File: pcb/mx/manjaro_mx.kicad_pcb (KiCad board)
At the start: 2 copper layers, 285.8 x 101 mm, 91 parts, among them SW1 SW_Push, SW10 SW_Push, SW11 SW_Push, SW12 SW_Push, SW13 SW_Push, SW14 SW_Push, SW15 SW_Push, SW16 SW_Push, SW17 SW_Push, SW18 SW_Push, SW19 SW_Push, SW2 SW_Push, SW20 SW_Push, SW21 SW_Push, SW22 SW_Push, SW3 SW_Push, SW4 SW_Push, SW5 SW_Push, SW6 SW_Push, SW7 SW_Push, SW8 SW_Push, SW9 SW_Push, U1 XIAO-RP2040-DIP

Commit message: [V0] add jlcpcb files
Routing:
- net rBAT-: track 182.9 -> 177.8 mm
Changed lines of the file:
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@@
 		(sheetname "ルート")
 		(sheetfile "manjaro_mx.kicad_sch")
-		(attr through_hole)
+		(attr through_hole exclude_from_bom dnp)
 		(fp_line
 			(start -2.06 -1.46)
@@
 		(sheetname "ルート")
 		(sheetfile "manjaro_mx.kicad_sch")
-		(attr through_hole)
+		(attr through_hole exclude_from_bom dnp)
 		(fp_line
 			(start -1.33 -1.33)
@@
 		(tags "connector JST PH top entry")
 		(property "Reference" "rBT1"
-			(at 1 -2.55 360)
+			(at 1 -2.55 0)
 			(layer "F.SilkS")
 			(effects
@@
 		)
 		(property "Value" "Battery_Cell"
-			(at 1 7.45 360)
+			(at 1 7.45 0)
 			(layer "F.Fab")
 			(effects
@@
 		(sheetname "ルート")
 		(sheetfile "manjaro_mx.kicad_sch")
-		(attr through_hole)
+		(attr through_hole exclude_from_bom dnp)
 		(fp_line
 			(start -2.06 -1.46)
@@
 		)
 		(fp_text user "${REFERENCE}"
-			(at 1 2.5 360)
+			(at 1 2.5 0)
 			(layer "F.Fab")
 			(effects
@@
 		)
 		(property "Value" "SW_Push"
-			(at 0.000001 7.8 15)
+			(at 0.000002 7.8 15)
 			(layer "B.Fab")
 			(hide yes)
@@
 				(xy 5.25 5.65) (xy 5.4 5.4) (xy 5.5 5) (xy 5.5 4.6) (xy 5.35 4.5) (xy 5.2 4.4) (xy 4.75 4.65) (xy 4.5 4.75)
 				(xy 4.05 4.85) (xy 3.55 4.85) (xy 2.95 4.7) (xy 2.45 4.4) (xy 2.15 4.15) (xy 1.75 3.6) (xy 1.55 3.05)
-				(xy 1.5 2.6) (xy 1.25 2.800001) (xy 0.899999 2.9) (xy 0.4 2.950001) (xy -1.65 2.95) (xy -1.2 3.2)
+				(xy 1.5 2.6) (xy 1.25 2.800001) (xy 0.899999 2.9) (xy 0.4 2.950002) (xy -1.65 2.95) (xy -1.2 3.2)
 				(xy -0.95 3.4) (xy -0.65 3.75) (xy -0.5 4) (xy -0.35 4.35) (xy -0.25 4.75) (xy -0.25 5.05) (xy -0.25 5.4)
 				(xy -0.3 5.65) (xy -0.45 6.05) (xy -0.75 6.5)
@@
 	)
 	(segment
-		(start 280 127.165)
-		(end 281.15 126.015)
+		(start 281.15 126.015)
+		(end 280 127.165)
 		(width 0.2)
 		(layer "B.Cu")
@@
 	)
 	(segment
-		(start 281.15 136.175)
-		(end 280 135.025)
+		(start 201.75 77.25)
+		(end 201.75 80)
 		(width 0.2)
 		(layer "B.Cu")
@@
 	)
 	(segment
-		(start 201.75 77.25)
-		(end 201.75 80)
+		(start 280 132.485)
+		(end 281.15 133.635)
 		(width 0.2)
 		(layer "B.Cu")
@@
 	)
 	(segment
-		(start 280 135.025)
-		(end 280 127.165)
-		(width 0.2)
-		(layer "B.Cu")
-		(net 27)
-	)
-	(segment
 		(start 191 82.46)
 		(end 191 106)
@@
 	)
 	(segment
-		(start 281.15 136.175)
-		(end 281.15 133.635)
+		(start 280 127.165)
+		(end 280 132.485)
 		(width 0.2)
 		(layer "B.Cu")

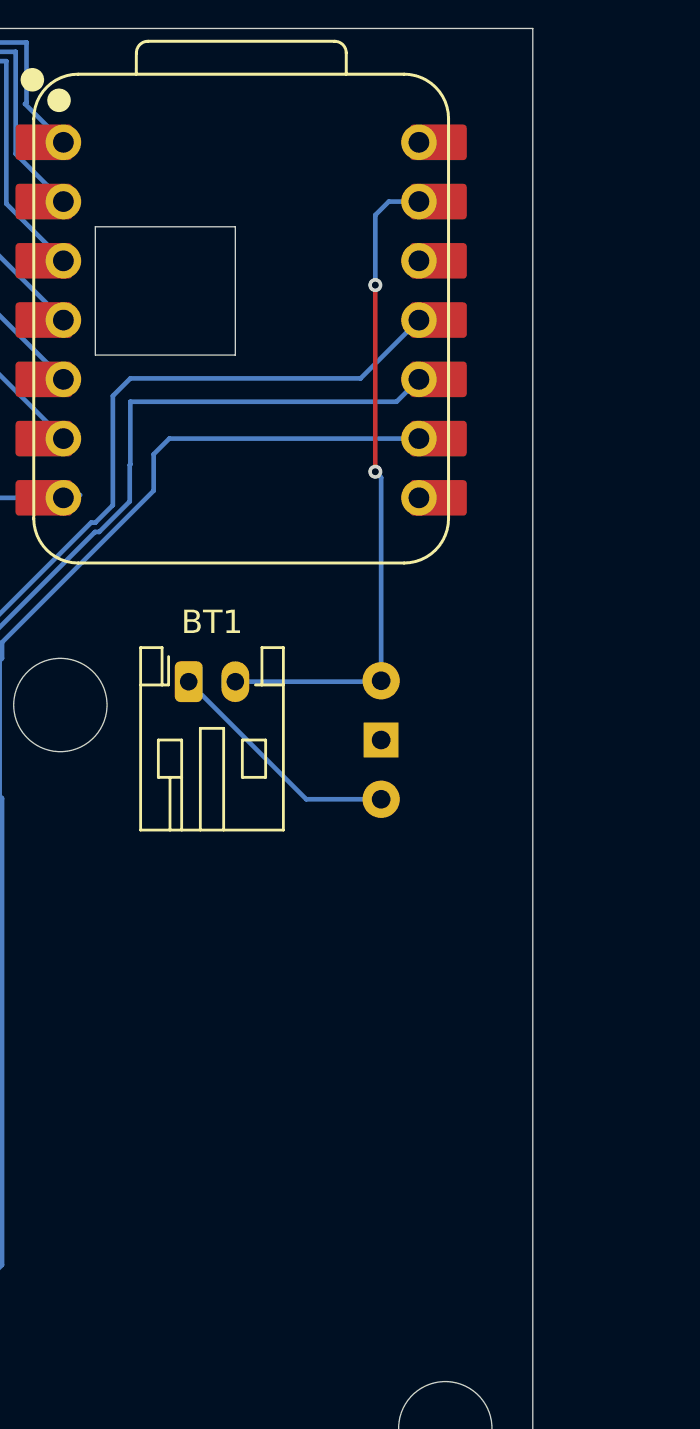
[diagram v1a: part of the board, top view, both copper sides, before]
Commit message: [V0] Add TRRS conn for mint right
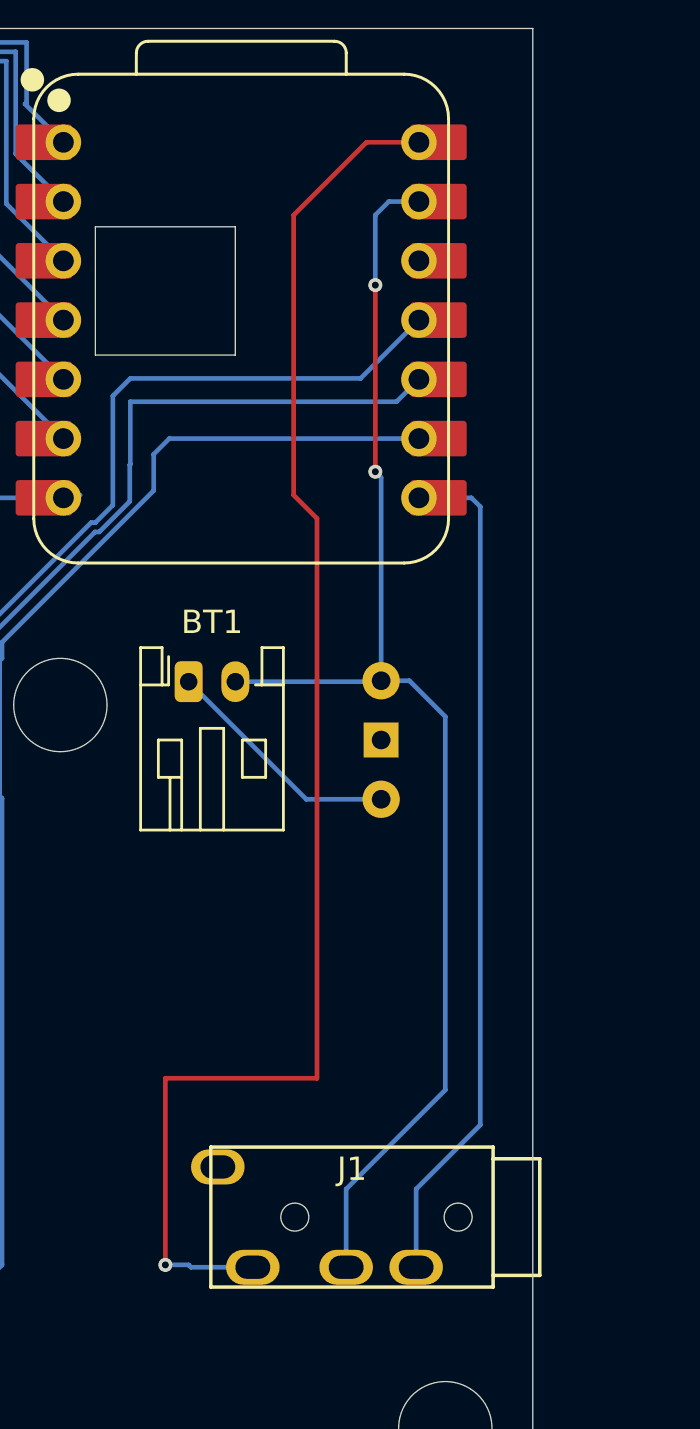
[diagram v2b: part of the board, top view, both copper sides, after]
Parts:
- added J1: MJ-4PP-9, MJ-4PP-9:MJ-4PP-9, F.Cu at (172.0, 103.0)
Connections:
- U1 pad 14: unconnected-(U1-VBUS-Pad14)_0 -> 5V
- U1 pad 8: unconnected-(U1-P1.12_RX_D7-Pad8)_0 -> TX
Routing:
- net 5V: track 0.00 -> 63.2 mm, vias 0 -> 1
- net TX: track 0.00 -> 36.5 mm
- net BAT-: track 28.4 -> 57.2 mm

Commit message: Modify key layout
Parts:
- removed J1: MJ-4PP-9, MJ-4PP-9:MJ-4PP-9
- added D23: 1N4148WT, digikey-footprints:SOD-523, B.Cu at (63.5, 140.2)
- added D24: 1N4148WT, digikey-footprints:SOD-523, B.Cu at (44.5, 142.2)
- added SW23: SW_Push, kbd_SW:CherryMX_Choc_Hotswap_1u, F.Cu at (69.0, 131.2)
- added SW24: SW_Push, kbd_SW:CherryMX_Choc_Hotswap_1u, F.Cu at (50.0, 133.2)
- added rD21: 1N4148WT, digikey-footprints:SOD-523, B.Cu at (291.7, 140.2)
- added rD22: 1N4148WT, digikey-footprints:SOD-523, B.Cu at (310.8, 142.2)
- added rSW21: SW_Push, kbd_SW:CherryMX_Choc_Hotswap_1u, F.Cu at (297.2, 131.2)
- added rSW22: SW_Push, kbd_SW:CherryMX_Choc_Hotswap_1u, F.Cu at (316.2, 133.2)
- D1, D10, D11, D12, D13, D14, D15, D16, D17, D18, D19, D2, D20, D21, D22, D3, D4, D5, D6, D7, D8, D9, rD1, rD10, rD11, rD12, rD13, rD14, rD15, rD16, rD17, rD18, rD19, rD2, rD20, rD3, rD4, rD5, rD6, rD7, rD8, rD9: footprint Diode_SMD:D_SOD-523 -> digikey-footprints:SOD-523
- SW1, SW10, SW11, SW12, SW13, SW14, SW15, SW16, SW17, SW18, SW19, SW2, SW20, SW21, SW22, SW3, SW4, SW5, SW6, SW7, SW8, SW9, rSW1, rSW10, rSW11, rSW12, rSW13, rSW14, rSW15, rSW16, rSW17, rSW18, rSW19, rSW2, rSW20, rSW3, rSW4, rSW5, rSW6, rSW7, rSW8, rSW9: footprint kbd:keyswitch_cherrymx_hotswap_1u -> kbd_SW:CherryMX_Choc_Hotswap_1u; moved to F.Cu
- U1, rU1: value XIAO-RP2040-DIP -> nice_nano; footprint Seeed Studio XIAO Series Library:XIAO-RP2040-DIP -> nice-nano-kicad:nice_nano
- moved rD19 119.5 mm to (205.8, 146.7), turned to 24 degrees
- moved rSW19 118.6 mm to (206.1, 136.1), turned to 24 degrees
- moved rSW6 95.3 mm to (316.2, 76.0), turned to 0 degrees
- moved rD6 89.7 mm to (310.8, 85.0)
- moved rSW16 87.1 mm to (278.1, 99.1), turned to 0 degrees
- moved rSW17 79.6 mm to (297.2, 112.1), turned to 0 degrees
- moved rD16 77.7 mm to (272.6, 108.1), turned to 180 degrees
- moved rSW11 76.7 mm to (297.2, 93.0), turned to 0 degrees
- moved rSW12 76.3 mm to (316.2, 95.0), turned to 0 degrees
- moved rD17 71.5 mm to (291.7, 121.1), turned to 180 degrees
- moved rD11 71.1 mm to (291.7, 102.0)
- moved rD12 70.4 mm to (310.8, 104.0)
- moved rD20 62.1 mm to (272.6, 127.2)
- moved rSW20 58.3 mm to (278.1, 118.2), turned to 0 degrees
- moved rD15 47.0 mm to (253.6, 104.1)
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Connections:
- U1 pad 1: COL5 -> unconnected-(U1-TX0/P0.06-Pad1)
- U1 pad 10: ROW2 -> COL3
- U1 pad 11: ROW1 -> COL4
- U1 pad 12: unconnected-(U1-3V3-Pad12) -> COL5
- U1 pad 13: BAT- -> unconnected-(U1-NFC1/P0.09-Pad13)
- U1 pad 14: 5V -> unconnected-(U1-NFC2/P0.10-Pad14)
- U1 pad 2: COL4 -> unconnected-(U1-RX1/P0.08-Pad2)
- U1 pad 3: COL3 -> BAT-
- U1 pad 4: COL2 -> BAT-
- U1 pad 5: COL1 -> unconnected-(U1-P0.17-Pad5)
- U1 pad 6: COL0 -> unconnected-(U1-P0.20-Pad6)
- U1 pad 7: ROW0 -> COL0
- U1 pad 8: TX -> COL1
- U1 pad 9: ROW3 -> COL2
- rJ3 pad 1: 3V3 -> r3V3
- rJ3 pad 5: rBAT- -> nCS
- rSW10 pad 2: rCOL4 -> rCOL3
- rSW11 pad 2: rCOL0 -> rCOL4
- rSW12 pad 2: rCOL1 -> rCOL5
- rSW13 pad 2: rCOL2 -> rCOL0
- rSW14 pad 2: rCOL3 -> rCOL1
- rSW15 pad 2: rCOL4 -> rCOL2
- rSW16 pad 2: rCOL0 -> rCOL3
- rSW17 pad 2: rCOL1 -> rCOL4
- rSW18 pad 2: rCOL2 -> rCOL5
- rSW19 pad 2: rCOL3 -> rCOL0
- rSW20 pad 2: rCOL4 -> rCOL1
- rSW6 pad 2: rCOL0 -> rCOL5
- rSW7 pad 2: rCOL1 -> rCOL0
- rSW8 pad 2: rCOL2 -> rCOL1
- rSW9 pad 2: rCOL3 -> rCOL2
- rU1 pad 1: rROW1 -> unconnected-(rU1-TX0/P0.06-Pad1)
- rU1 pad 10: rROW2 -> rCOL3
- rU1 pad 11: SDIO -> rCOL4
- rU1 pad 12: 3V3 -> rCOL5
- rU1 pad 13: rBAT- -> unconnected-(rU1-NFC1/P0.09-Pad13)
- rU1 pad 2: rCOL4 -> unconnected-(rU1-RX1/P0.08-Pad2)
- rU1 pad 3: rCOL3 -> rBAT-
- rU1 pad 4: rCOL2 -> rBAT-
- rU1 pad 5: rCOL1 -> unconnected-(rU1-P0.17-Pad5)
- rU1 pad 6: rCOL0 -> unconnected-(rU1-P0.20-Pad6)
- rU1 pad 7: rROW0 -> rCOL0
- rU1 pad 8: rROW3 -> rCOL1
- rU1 pad 9: SCLK -> rCOL2
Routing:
- net rROW3: track 258.2 -> 0.00 mm, vias 8 -> 0
- net rCOL2: track 202.2 -> 0.00 mm, vias 4 -> 0
- net rCOL3: track 196.9 -> 0.00 mm, vias 4 -> 0
- net rCOL4: track 195.8 -> 0.00 mm
- net rBAT-: track 177.8 -> 0.00 mm, vias 2 -> 0
- net COL3: track 176.8 -> 0.00 mm
- net ROW3: track 176.8 -> 0.00 mm, vias 8 -> 0
- net COL5: track 175.4 -> 0.00 mm, vias 2 -> 0
- net ROW2: track 175.0 -> 0.00 mm, vias 8 -> 0
- net rROW1: track 168.4 -> 0.00 mm, vias 10 -> 0
- net 3V3: track 167.3 -> 0.00 mm, vias 1 -> 0
- net ROW1: track 165.7 -> 0.00 mm, vias 10 -> 0
- net COL2: track 160.4 -> 0.00 mm
- net COL4: track 159.7 -> 0.00 mm, vias 2 -> 0
- net rCOL1: track 153.4 -> 0.00 mm, vias 2 -> 0
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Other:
- board size 285.8 x 101 mm -> 289 x 116 mm
- board text added: "Manjaro v1"

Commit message: Modify MCU position
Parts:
- added EXSW1: RotaryEncoder_Switch, Keebio-Parts:RotaryEncoder_EC11, F.Cu at (164.3, 108.1)
- added rEXSW1: RotaryEncoder_Switch, Keebio-Parts:RotaryEncoder_EC11, F.Cu at (201.9, 108.1)
- moved U1 107.3 mm to (60.0, 56.0), turned to 0 degrees
- moved rU1 106.3 mm to (306.0, 56.0), turned to 180 degrees
- moved rPowerSW1 62.4 mm to (240.1, 51.0), turned to 0 degrees
- moved PowerSW1 62.2 mm to (126.2, 51.0), turned to 0 degrees
- moved rBT1 48.1 mm to (228.0, 51.0), turned to -90 degrees
- moved BT1 45.1 mm to (138.2, 53.0), turned to 90 degrees
- moved rJ3 7.88 mm to (262.0, 130.8)
- moved SW20 3.16 mm to (137.2, 130.1), turned to 0 degrees
- moved D1 3.00 mm to (139.8, 79.0)
- moved D13 3.00 mm to (139.8, 117.1)
- moved D19 3.00 mm to (151.8, 140.3), turned to 165 degrees
- moved D7 3.00 mm to (139.8, 98.0)
- moved SW1 3.00 mm to (145.2, 70.0)
- moved SW13 3.00 mm to (145.2, 108.1)
- moved SW19 3.00 mm to (160.2, 133.1), turned to -15 degrees
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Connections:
- U1 pad 15: unconnected-(U1-P1.11-Pad15) -> KEYEX1
- U1 pad 5: unconnected-(U1-P0.17-Pad5) -> REB
- U1 pad 6: unconnected-(U1-P0.20-Pad6) -> RE0A
- rU1 pad 15: unconnected-(rU1-P1.11-Pad15) -> rKEYEX1
- rU1 pad 5: unconnected-(rU1-P0.17-Pad5) -> rREB
- rU1 pad 6: unconnected-(rU1-P0.20-Pad6) -> rRE0A
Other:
- board size 289 x 116 mm -> 286 x 116 mm

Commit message: fixed external line
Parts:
- removed EXSW1, rEXSW1: RotaryEncoder_Switch, Keebio-Parts:RotaryEncoder_EC11
- added ?: , , F.Cu at (226.0, 45.0)
- added ?: , , F.Cu at (230.0, 45.0)
- added ?: , , F.Cu at (227.0, 45.0)
- added ?: , , F.Cu at (134.0, 45.0)
- added ?: , , F.Cu at (229.0, 45.0)
- added ?: , , F.Cu at (82.0, 45.0)
- added ?: , , F.Cu at (131.0, 45.0)
- added ?: , , F.Cu at (133.0, 45.0)
- added ?: , , F.Cu at (278.0, 45.0)
- added ?: , , F.Cu at (81.0, 45.0)
- added ?: , , F.Cu at (277.0, 45.0)
- added ?: , , F.Cu at (83.0, 45.0)
- added ?: , , F.Cu at (276.0, 45.0)
- added ?: , , F.Cu at (280.0, 45.0)
- added ?: , , F.Cu at (279.0, 45.0)
- added ?: , , F.Cu at (132.0, 45.0)
- added ?: , , F.Cu at (80.0, 45.0)
- added ?: , , F.Cu at (130.0, 45.0)
- added ?: , , F.Cu at (84.0, 45.0)
- added ?: , , F.Cu at (228.0, 45.0)
- D1, D10, D11, D12, D13, D14, D15, D16, D17, D18, D19, D2, D20, D21, D22, D23, D24, D3, D4, D5, D6, D7, D8, D9, rD1, rD10, rD11, rD12, rD13, rD14, rD15, rD16, rD17, rD18, rD19, rD2, rD20, rD21, rD22, rD3, rD4, rD5, rD6, rD7, rD8, rD9: footprint digikey-footprints:SOD-523 -> Keebio-Parts:D_SOD-323
- PowerSW1, rPowerSW1: moved to F.Cu
- SW1, SW10, SW11, SW12, SW13, SW14, SW15, SW16, SW17, SW18, SW19, SW2, SW20, SW21, SW22, SW23, SW24, SW3, SW4, SW5, SW6, SW7, SW8, SW9, rSW1, rSW10, rSW11, rSW12, rSW13, rSW14, rSW15, rSW16, rSW17, rSW18, rSW19, rSW2, rSW20, rSW21, rSW22, rSW3, rSW4, rSW5, rSW6, rSW7, rSW8, rSW9: footprint kbd_SW:CherryMX_Choc_Hotswap_1u -> kbd_SW:Choc_Hotswap_1u
- moved rD19 9.78 mm to (196.0, 144.0)
- moved rSW19 6.32 mm to (200.1, 135.1)
- moved rD21 6.08 mm to (285.7, 141.2)
- moved rD22 6.08 mm to (304.8, 143.2)
- moved rSW15 6.00 mm to (253.1, 95.1)
- moved rSW3 6.00 mm to (253.1, 57.0)
- moved rSW9 6.00 mm to (253.1, 76.0)
- moved rBT1 6.00 mm to (222.0, 51.0)
- moved rD1 6.00 mm to (209.5, 79.0)
- moved rD10 6.00 mm to (266.6, 89.0)
- moved rD11 6.00 mm to (285.7, 104.0)
- moved rD12 6.00 mm to (304.8, 106.0)
- moved rD13 6.00 mm to (209.5, 116.1)
- moved rD14 6.00 mm to (228.6, 115.1)
- moved rD15 6.00 mm to (247.6, 104.1)
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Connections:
- U1 pad 15: KEYEX1 -> unconnected-(U1-P1.11-Pad15)
- U1 pad 5: REB -> unconnected-(U1-P0.17-Pad5)
- U1 pad 6: RE0A -> unconnected-(U1-P0.20-Pad6)
- rU1 pad 15: rKEYEX1 -> unconnected-(rU1-P1.11-Pad15)
- rU1 pad 5: rREB -> unconnected-(rU1-P0.17-Pad5)
- rU1 pad 6: rRE0A -> unconnected-(rU1-P0.20-Pad6)
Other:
- board size 286 x 116 mm -> 281 x 113 mm

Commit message: fixed keylayout & MCU position
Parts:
- removed ? (x20): , 
- removed D23, D24: 1N4148WT, Keebio-Parts:D_SOD-323
- removed SW23, SW24: SW_Push, kbd_SW:Choc_Hotswap_1u
- added EXSW1: RotaryEncoder_Switch, Keebio-Parts:RotaryEncoder_EC11, F.Cu at (166.0, 108.1)
- added rEXSW1: RotaryEncoder_Switch, Keebio-Parts:RotaryEncoder_EC11, F.Cu at (193.0, 108.1)
- moved rU1 107.4 mm to (193.0, 65.0), turned to -90 degrees
- moved U1 106.4 mm to (166.0, 65.0), turned to -90 degrees
- moved rSW20 55.7 mm to (218.0, 131.1), turned to 15 degrees
- moved rD20 53.5 mm to (215.0, 141.3), turned to 15 degrees
- moved rD21 41.8 mm to (248.1, 123.0)
- moved rSW21 41.7 mm to (254.1, 114.2)
- moved rD22 41.0 mm to (267.1, 127.0)
- moved rSW22 40.8 mm to (273.1, 118.2)
- moved rPowerSW1 14.0 mm to (220.1, 51.0)
- moved PowerSW1 13.8 mm to (140.0, 51.0)
- moved BT1 12.3 mm to (127.0, 48.0), turned to -90 degrees
- moved rJ3 10.8 mm to (268.0, 132.8)
- moved rBT1 9.06 mm to (231.0, 50.0), turned to 90 degrees
- moved SW20 5.10 mm to (142.2, 131.1), turned to -15 degrees
- moved rD19 4.73 mm to (196.0, 148.7), turned to 24 degrees
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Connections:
- U1 pad 15: unconnected-(U1-P1.11-Pad15) -> KEYEX1
- U1 pad 5: unconnected-(U1-P0.17-Pad5) -> REB
- U1 pad 6: unconnected-(U1-P0.20-Pad6) -> RE0A
- rU1 pad 15: unconnected-(rU1-P1.11-Pad15) -> rKEYEX1
- rU1 pad 5: unconnected-(rU1-P0.17-Pad5) -> rREB
- rU1 pad 6: unconnected-(rU1-P0.20-Pad6) -> rRE0A
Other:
- board size 281 x 113 mm -> 283 x 118 mm
- board text removed: "Manjaro v0"

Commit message: Fixed v1 layout
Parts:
- removed rD22: 1N4148WT, Keebio-Parts:D_SOD-323
- removed rSW22: SW_Push, kbd_SW:Choc_Hotswap_1u
- added D23: 1N4148WT, Keebio-Parts:D_SOD-323, B.Cu at (68.5, 137.9)
- added J2: MJ-4PP-9, MJ-4PP-9:MJ-4PP-9, F.Cu at (164.5, 118.0)
- added SW23: SW_Push, kbd:keyswitch_cherrymx_hotswap_1u, B.Cu at (63.0, 133.2)
- added rJ2: MJ-4PP-9, MJ-4PP-9:MJ-4PP-9, F.Cu at (191.0, 118.0)
- SW1, SW10, SW11, SW12, SW13, SW14, SW15, SW16, SW17, SW18, SW19, SW2, SW20, SW21, SW22, SW3, SW4, SW5, SW6, SW7, SW8, SW9, rSW1, rSW10, rSW11, rSW12, rSW13, rSW14, rSW15, rSW16, rSW17, rSW18, rSW19, rSW2, rSW20, rSW21, rSW3, rSW4, rSW5, rSW6, rSW7, rSW8, rSW9: footprint kbd_SW:Choc_Hotswap_1u -> kbd:keyswitch_cherrymx_hotswap_1u; moved to B.Cu
- moved rSW21 42.6 mm to (292.2, 133.2), turned to 180 degrees
- moved rD21 41.4 mm to (286.7, 137.9), turned to 90 degrees
- moved rJ3 11.1 mm to (276.1, 125.3)
- moved EXSW1 10.7 mm to (161.0, 98.6)
- moved rEXSW1 9.50 mm to (193.0, 98.6)
- moved D1 7.21 mm to (144.8, 75.0), turned to 90 degrees
- moved D10 7.21 mm to (87.6, 85.0), turned to 90 degrees
- moved D11 7.21 mm to (68.5, 100.0), turned to 90 degrees
- moved D12 7.21 mm to (49.5, 102.0), turned to 90 degrees
- moved D13 7.21 mm to (144.8, 113.1), turned to 90 degrees
- moved D14 7.21 mm to (125.7, 111.1), turned to 90 degrees
- moved D15 7.21 mm to (106.7, 100.1), turned to 90 degrees
- moved D16 7.21 mm to (87.6, 104.1), turned to 90 degrees
- moved D17 7.21 mm to (68.5, 119.1), turned to 90 degrees
- moved D18 7.21 mm to (49.5, 121.1), turned to 90 degrees
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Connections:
- net r3V3 renamed rVCC
- U1 pad 1: unconnected-(U1-TX0/P0.06-Pad1) -> KEYEX1
- U1 pad 15: KEYEX1 -> unconnected-(U1-P1.11-Pad15)
- U1 pad 2: unconnected-(U1-RX1/P0.08-Pad2) -> DATA
- U1 pad 21: unconnected-(U1-VCC-Pad21) -> VCC
- rJ3 pad 5: nCS -> NCS
- rU1 pad 1: unconnected-(rU1-TX0/P0.06-Pad1) -> rKEYEX1
- rU1 pad 13: unconnected-(rU1-NFC1/P0.09-Pad13) -> NCS
- rU1 pad 15: rKEYEX1 -> SDIO
- rU1 pad 16: unconnected-(rU1-P1.13-Pad16) -> SCLK
- rU1 pad 2: unconnected-(rU1-RX1/P0.08-Pad2) -> rDATA
- rU1 pad 31: nCS -> unconnected-(rU1-P1.01-Pad31)
- rU1 pad 32: SDIO -> unconnected-(rU1-P1.02-Pad32)
- rU1 pad 33: SCLK -> unconnected-(rU1-P1.07-Pad33)
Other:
- board size 283 x 118 mm -> 286.5 x 113.5 mm

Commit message: fiexed layout
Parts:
- moved D19 2.00 mm to (162.5, 144.5)
- moved D20 2.00 mm to (143.5, 137.5)
- moved SW19 2.00 mm to (159.2, 138.1)
- moved SW20 2.00 mm to (139.2, 131.1)
- moved rD19 2.00 mm to (193.0, 144.7)
- moved rD20 2.00 mm to (212.0, 137.3)
- moved rJ3 2.00 mm to (276.1, 127.3)
- moved rSW19 2.00 mm to (196.0, 138.1)
- moved rSW20 2.00 mm to (216.0, 131.1)
- moved D1 1.00 mm to (144.8, 74.0)
- moved D11 1.00 mm to (68.5, 99.0)
- moved D12 1.00 mm to (49.5, 101.0)
- moved D13 1.00 mm to (144.8, 112.1)
- moved D14 1.00 mm to (125.7, 110.1)
- moved D17 1.00 mm to (68.5, 118.1)
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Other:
- outline, holes or cut-outs redrawn
